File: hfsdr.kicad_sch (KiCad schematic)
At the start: 41 parts, among them U2 ADA4938-1

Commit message: wokrin
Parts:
- added C31, C32: 0.1u, Capacitor_SMD:C_0402_1005Metric, symbol Device:C
- added C33, C35, C36, C37, C38, C39, C40, C41, C42, C43, C48, C53, C54: 0.1uF, Capacitor_SMD:C_0402_1005Metric, symbol Device:C
- added C34, C44, C45, C46, C47, C49, C50: 1uF, Capacitor_SMD:C_0402_1005Metric, symbol Device:C
- added C51, C52: 0.1n, Capacitor_SMD:C_0402_1005Metric, symbol Device:C
- added R10, R12, R13: 50k, Resistor_SMD:R_0402_1005Metric, symbol Device:R_US
- added R11, R15, R16, R18, R19, R20: 10k, Resistor_SMD:R_0402_1005Metric, symbol Device:R_US
- added R14: 100, Resistor_SMD:R_0402_1005Metric, symbol Device:R_US
- added R17: 4.12k, Resistor_SMD:R_0402_1005Metric, symbol Device:R_US
- added U3: ~, symbol hfsdr:590BD80M0000DG
- added U4: AD9515, Package_CSP:LFCSP-32-1EP_5x5mm_P0.5mm_EP3.1x3.1mm, symbol Timer:AD9515
- added U5, U6: ~, symbol hfsdr:NCP110AMX180TBG
- added U7: ~, symbol hfsdr:TLV77333PDBVR
- R1: value 200 -> 402
- R2: value 120 -> 402
- R7: value 200 -> 127
- R8: value 90 -> 127
- R9: value 63.4 -> 50k
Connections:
- net DRGND is gone; now on net AGND: C19.2, C20.2, C21.2, C22.2, C23.2, C24.2, C25.2, C26.2, U1.11 (DRGND), U1.13 (DRGND), U1.17 (DRGND)
- net AGND: now also R9.2, C33.2, C34.2, C35.2, C36.2, C37.2, C38.2, C39.2, C40.2, C41.2, C42.2, C43.2, C44.2, C45.2, C46.2, C47.2, C48.1, C49.2, C50.2, R10.1, R12.2, R13.2, R17.1, U3.3 (GND), U4.10 (S7), U4.12 (S5), U4.13 (S4), U4.14 (S3), U4.15 (S2), U4.16 (S1), U4.25 (S0), U4.31 (GND), U4.33 (GND), U4.7 (S10), U4.8 (S9), U4.9 (S8), U5.B2 (GND), U6.B2 (GND), U7.2 (GND); no longer R2.1, R9.1
- net AVDD: now also C45.1, U5.A2 (OUT)
- net DRVDD: now also C47.1, U6.A2 (OUT)
- net at R8.2, U2.3 (-): now also R1.1; no longer R7.1
- net at R7.2: now also R2.1, U2.2 (+); no longer U2.1 (FB-)
- net at R3.1, U2.10: no longer R1.1
- net at U1.4 (CLK+): now also C54.1
- net at U1.5 (CLK-): now also C53.1
- net at U2.12 (~{PD}): now also R20.1
- net at U2.5 (V+), U2.6 (V+), U2.7 (V+)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: now also R20.2
- net at U2.4 (FB+): now also R2.2
- net VIN: no longer names the net of R8.1
- net VIN: no longer R9.2
- new net: C52.1, R12.1, U4.23 (OUT0)
- new net: C32.1, R10.2, U3.5 (CLK-)
- new net: R16.2, U6.B1 (EN)
- new net: C31.1, R9.1, U3.4 (CLK+)
- new net: C31.2, U4.2 (CLK)
- new net: R1.2, U2.1 (FB-)
- new net: C32.2, U4.3 (CLKB)
- new net: R18.1, U4.5 (SYNCB)
- new net: R11.1, U3.2 (OE)
- new net: C51.1, R13.1, U4.22 (OUT0B)
- new net: R17.2, U4.32 (RSET)
- new net: R15.2, U5.B1 (EN)
- new net: R19.2, U7.3 (EN)
- new net +5V: C44.1, C46.1, C49.1, R15.1, R16.1, R19.1, U5.A1 (IN), U6.A1 (IN), U7.1 (IN)
- new net CLK+: C52.2, C54.2, R14.2
- new net CLK-: C51.2, C53.2, R14.1
- new net CLKVDD: C33.1, C34.1, C35.1, C36.1, C37.1, C38.1, C39.1, C40.1, C41.1, C42.1, C43.1, C48.2, C50.1, R11.2, R18.2, U3.6 (VDD), U4.1 (VS), U4.11 (S6), U4.17 (VS), U4.20 (VS), U4.21 (VS), U4.24 (VS), U4.26 (VS), U4.29 (VS), U4.30 (VS), U4.4 (VS), U7.5 (OUT)
- no-connect marks 0 -> 4
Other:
- note added: "100 ohm diff trx line"
- note added: "10dB gain driver stage"
- note added: "input impedance of Rg * 2 for diff balanced (127)"
- note added: "term resistor close as possible"
- note added: "uhh"
- moved on the sheet: C27, C28, C29, C30, R1, R2, R3, R4, R5, R6, R7, R8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

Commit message: update
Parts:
- added C55, C60: 1uF, Capacitor_SMD:C_0402_1005Metric, symbol Device:C
- added C56, C61: 2.2uF, Capacitor_SMD:C_0402_1005Metric, symbol Device:C
- added C57, C58, C59: 0.1uF, Capacitor_SMD:C_0402_1005Metric, symbol Device:C
- added R21, R22, R23, R24, R25, R26, R27, R28: 10k, Resistor_SMD:R_0402_1005Metric, symbol Device:R_US
- added R29: 25k, Resistor_SMD:R_0402_1005Metric, symbol Device:R_US
- added R30: 50k, Resistor_SMD:R_0402_1005Metric, symbol Device:R_US
- added U10, U9: ~, Package_TO_SOT_SMD:SOT-89-3, symbol hfsdr:AP2205-50Y-13
- added U8: ~, Package_CSP:LFCSP-20-1EP_4x4mm_P0.5mm_EP2.1x2.1mm, symbol hfsdr:ADL5206
- R1, R2: value 402 -> 250
- R7, R8: value 127 -> 50
- U1: footprint (none) -> Package_CSP:LFCSP-32-1EP_5x5mm_P0.5mm_EP3.6x3.6mm_ThermalVias
- U5, U6: footprint (none) -> Package_DFN_QFN:OnSemi_XDFN4-1EP_1.0x1.0mm_EP0.52x0.52mm
- U7: footprint (none) -> Package_TO_SOT_SMD:SOT-23-5
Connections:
- net AGND: now also C55.2, C56.2, C57.2, C58.2, C59.1, C60.2, C61.2, R22.1, R24.1, R26.1, R27.1, R28.1, R30.2, U10.2 (GND), U8.0 (EP), U9.2 (GND); no longer U4.10 (S7), U4.12 (S5), U4.13 (S4), U4.14 (S3), U4.15 (S2), U4.16 (S1), U4.25 (S0), U4.7 (S10), U4.8 (S9), U4.9 (S8)
- net CLKVDD: now also R23.1; no longer C48.2, U4.11 (S6)
- net at R7.1: now also U8.15 (VOUT+)
- net -5V: now reaches U2.13 (V-), U2.14 (V-), U2.15 (V-), U2.16 (V-)
- net at R20.2, U2.5 (V+), U2.6 (V+)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: now also C61.1, U10.3 (VOUT)
- net at R8.1: now also U8.14 (VOUT-)
- net VIN+ renamed ADCIN+
- net VIN- renamed ADCIN-
- new net: R22.2, U4.10 (S7), U4.12 (S5), U4.13 (S4), U4.14 (S3), U4.15 (S2), U4.16 (S1), U4.25 (S0), U4.7 (S10), U4.8 (S9), U4.9 (S8)
- new net: R26.2, U8.11 (LATCH/SPI_HP_LP)
- new net: R21.2, U8.13 (PWUP)
- new net: R29.2, R30.1, U8.19 (VPOS)
- new net: C48.2, R23.2, U4.11 (S6)
- new net: R28.2, U8.7 (FA/GS0/D2)
- new net: C59.2, U8.1 (VCM)
- new net: R24.2, U8.2 (MODE1)
- new net: R25.2, U8.3 (MODE0)
- new net: R27.2, U8.9 (UPDN_DAT/D0/3SPI_4SPI)
- new net +13.8V: C55.1, C60.1, U10.1 (VIN), U9.1 (VIN)
- new net AMPIN+: U8.17 (VIN+)
- new net AMPIN-: U8.18 (VIN-)
- new net VGA_CSB: U8.6 (CS/GS1/D3)
- new net VGA_VDD: C56.1, C57.1, C58.1, R21.1, R25.1, R29.1, U8.16 (VPOS), U8.19 (VPOS), U9.3 (VOUT)
- no-connect marks 4 -> 5
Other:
- note added: "14dB gain driver stage"
- note added: "add filtering between amps?"
- note added: "antialias lpf"
- note added: "bpfs?"
- note added: "check the datasheet???"
- note added: "close to driver"
- note added: "input"
- note added: "input impedance of Rg * 2 for diff balanced (100)"
- note added: "place close as possible to pins"
- note added: "private ADC supply"
- note added: "pull to +5v for 4 wire"
- note added: "set up in SPI 3 wire mode"
- note removed: "10dB gain driver stage"
- note removed: "input impedance of Rg * 2 for diff balanced (127)"
- note removed: "uhh"
- moved on the sheet: C27, C28, C29, C30, C48, C51, C52, C53, C54, R1, R12, R13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

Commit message: pcb ready
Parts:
- added C62: 120p, Capacitor_SMD:C_0402_1005Metric, symbol Device:C
- added C63, C64: 200p, Capacitor_SMD:C_0402_1005Metric, symbol Device:C
- added C65: 160p, Capacitor_SMD:C_0402_1005Metric, symbol Device:C
- added C66: 470n, Capacitor_SMD:C_0402_1005Metric, symbol Device:C
- added C67, C68: 0.1u, Capacitor_SMD:C_0402_1005Metric, symbol Device:C
- added J1: RFIN, Connector_Coaxial:SMA_Amphenol_132289_EdgeMount, symbol Connector:Conn_Coaxial_Small
- added L1: 390n, Inductor_SMD:L_0402_1005Metric, symbol Device:L
- added L2: 470n, Inductor_SMD:L_0402_1005Metric, symbol Device:L
- added L3: 510n, Inductor_SMD:L_0402_1005Metric, symbol Device:L
- added L4: 300n, Inductor_SMD:L_0402_1005Metric, symbol Device:L
- U3: footprint (none) -> hfsdr:SI590_5x7mm
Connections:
- net +5V: now also U5.4 (IN), U6.4 (IN); no longer U5.A1 (IN), U6.A1 (IN)
- net AGND: now also U1.33 (AGND), U5.2 (GND), U5.5 (EP), U6.2 (GND), U6.5 (EP), U8.21 (EP), C62.2, C63.2, C64.2, C65.2, C68.1, J1.2 (Ext); no longer U1.0 (AGND), U5.B2 (GND), U6.B2 (GND), U8.0 (EP)
- net AMPIN+: now also C67.2
- net AMPIN-: now also C68.2
- net AVDD: now also U5.1 (OUT); no longer U5.A2 (OUT)
- net DRVDD: now also U6.1 (OUT); no longer U6.A2 (OUT)
- net at R16.2: now also U6.3 (EN); no longer U6.B1 (EN)
- net at R29.2, R30.1: now also U8.20 (DNC_INTERIM); no longer U8.19 (VPOS)
- net at R15.2: now also U5.3 (EN); no longer U5.B1 (EN)
- new net: C65.1, L3.2, L4.1
- new net: C62.1, C66.2, L1.1
- new net: C67.1, L4.2
- new net: C64.1, L2.2, L3.1
- new net: C66.1, J1.1 (In)
- new net: C63.1, L1.2, L2.1
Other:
- note added: "amphenol 132289"
- note removed: "antialias lpf"
- note removed: "bpfs?"
- note removed: "input"

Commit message: dgfsd
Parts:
- added C69: 0.1uF, Capacitor_SMD:C_0402_1005Metric, symbol Device:C
- U10, U9: value ~ -> AP2205-50Y-13
- U7: value ~ -> TLV77333PDBVR
- U8: value ~ -> ADL5206
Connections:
- net AGND: now also R23.1, C69.1; no longer C19.2, C20.2, C21.2, C22.2, C23.2, C24.2, C25.2, C26.2
- net CLKVDD: no longer R23.1
- net at C61.1, R20.2, U10.3 (VOUT)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: now also C69.2
- new net DRGND: C19.2, C20.2, C21.2, C22.2, C23.2, C24.2, C25.2, C26.2
- no-connect marks 5 -> 17
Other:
- moved on the sheet: R27, R28

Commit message: asd
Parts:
- removed C28, C30: 15pF, Capacitor_SMD:C_0402_1005Metric, symbol Device:C
- removed R5: 33, Resistor_SMD:R_0402_1005Metric, symbol Device:R_US
- removed R6: 15, Resistor_SMD:R_0402_1005Metric, symbol Device:R_US
- added D1: ESD9B3.3ST5G, Diode_SMD:D_SOD-923, symbol Diode:ESD9B3.3ST5G
- added L5, L6: 30n, Inductor_SMD:L_0402_1005Metric, symbol Device:L
- C29: value 5pF -> 47pF
- R3: value 33 -> 24.3
- R4: value 15 -> 24.3
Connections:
- net ADCIN+: now also C29.2, L6.2; no longer R4.2
- net ADCIN-: now also C29.1, L5.2
- net AGND: now also D1.1 (A1)
- net at U2.11: now also R4.1
- net at C66.1, J1.1 (In): now also D1.2 (A2)
- new net: L5.1, R4.2
- new net: L6.1, R3.2
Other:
- note removed: "add filtering between amps?"
- moved on the sheet: C29, C62, C63, C64, C65, C66, C67, C68, J1, L1, L2, L3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

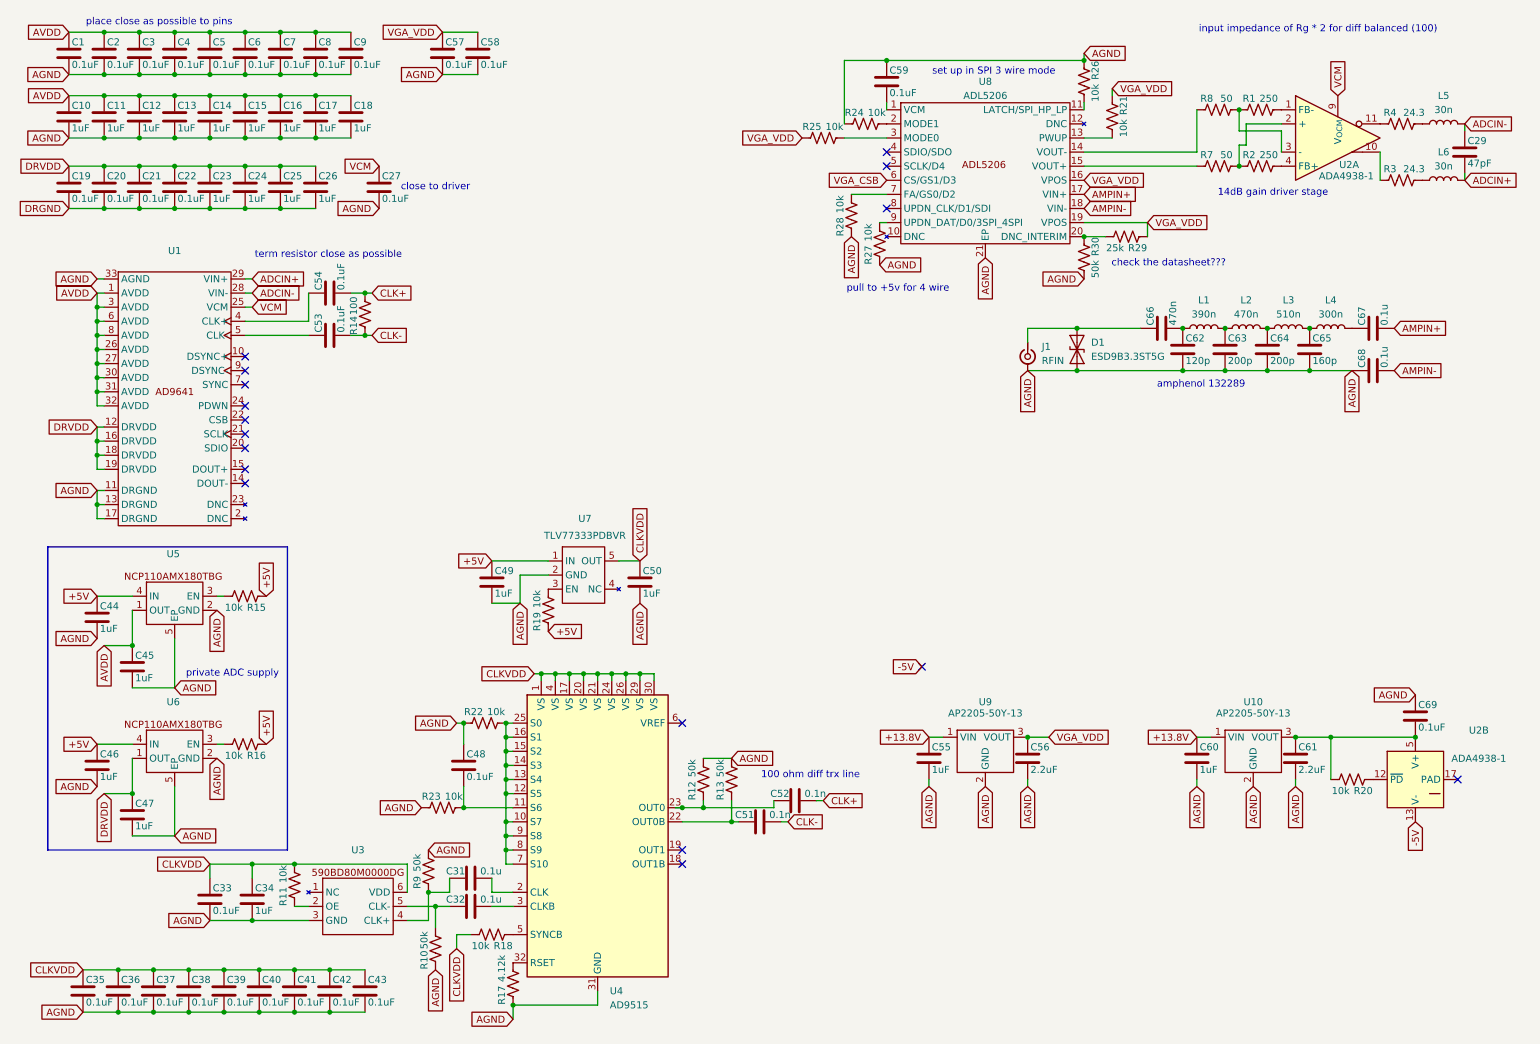
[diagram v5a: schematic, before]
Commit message: setup usbc
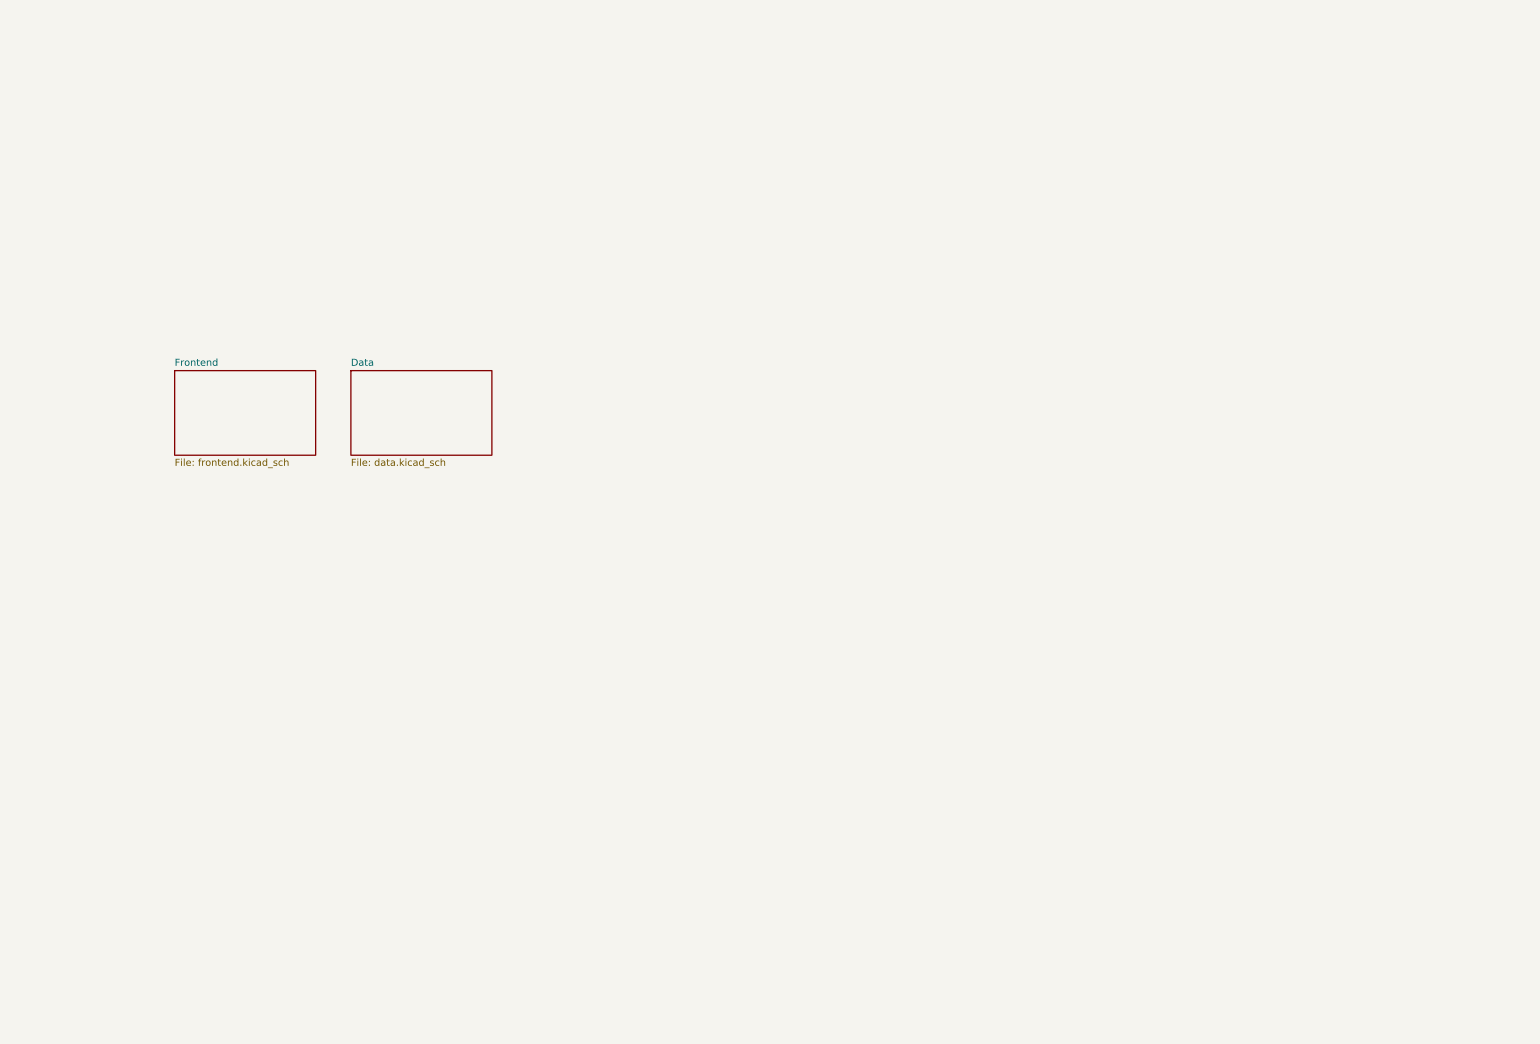
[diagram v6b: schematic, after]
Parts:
- removed C1, C19, C2, C20, C21, C22, C27, C3, C33, C35, C36, C37, C38, C39, C4, C40, C41, C42, C43, C48, C5, C53, C54, C57, C58, C59, C6, C69, C7, C8, C9: 0.1uF, Capacitor_SMD:C_0402_1005Metric, symbol Device:C
- removed C10, C11, C12, C13, C14, C15, C16, C17, C18, C23, C24, C25, C26, C34, C44, C45, C46, C47, C49, C50, C55, C60: 1uF, Capacitor_SMD:C_0402_1005Metric, symbol Device:C
- removed C29: 47pF, Capacitor_SMD:C_0402_1005Metric, symbol Device:C
- removed C31, C32, C67, C68: 0.1u, Capacitor_SMD:C_0402_1005Metric, symbol Device:C
- removed C51, C52: 0.1n, Capacitor_SMD:C_0402_1005Metric, symbol Device:C
- removed C56, C61: 2.2uF, Capacitor_SMD:C_0402_1005Metric, symbol Device:C
- removed C62: 120p, Capacitor_SMD:C_0402_1005Metric, symbol Device:C
- removed C63, C64: 200p, Capacitor_SMD:C_0402_1005Metric, symbol Device:C
- removed C65: 160p, Capacitor_SMD:C_0402_1005Metric, symbol Device:C
- removed C66: 470n, Capacitor_SMD:C_0402_1005Metric, symbol Device:C
- removed D1: ESD9B3.3ST5G, Diode_SMD:D_SOD-923, symbol Diode:ESD9B3.3ST5G
- removed J1: RFIN, Connector_Coaxial:SMA_Amphenol_132289_EdgeMount, symbol Connector:Conn_Coaxial_Small
- removed L1: 390n, Inductor_SMD:L_0402_1005Metric, symbol Device:L
- removed L2: 470n, Inductor_SMD:L_0402_1005Metric, symbol Device:L
- removed L3: 510n, Inductor_SMD:L_0402_1005Metric, symbol Device:L
- removed L4: 300n, Inductor_SMD:L_0402_1005Metric, symbol Device:L
- removed L5, L6: 30n, Inductor_SMD:L_0402_1005Metric, symbol Device:L
- removed R1, R2: 250, Resistor_SMD:R_0402_1005Metric, symbol Device:R_US
- removed R10, R12, R13, R30, R9: 50k, Resistor_SMD:R_0402_1005Metric, symbol Device:R_US
- removed R11, R15, R16, R18, R19, R20, R21, R22, R23, R24, R25, R26, R27, R28: 10k, Resistor_SMD:R_0402_1005Metric, symbol Device:R_US
- removed R14: 100, Resistor_SMD:R_0402_1005Metric, symbol Device:R_US
- removed R17: 4.12k, Resistor_SMD:R_0402_1005Metric, symbol Device:R_US
- removed R29: 25k, Resistor_SMD:R_0402_1005Metric, symbol Device:R_US
- removed R3, R4: 24.3, Resistor_SMD:R_0402_1005Metric, symbol Device:R_US
- removed R7, R8: 50, Resistor_SMD:R_0402_1005Metric, symbol Device:R_US
- removed U1: ~, Package_CSP:LFCSP-32-1EP_5x5mm_P0.5mm_EP3.6x3.6mm_ThermalVias, symbol hfsdr:AD9641
- removed U10, U9: AP2205-50Y-13, Package_TO_SOT_SMD:SOT-89-3, symbol hfsdr:AP2205-50Y-13
- removed U2: ADA4938-1, Package_CSP:LFCSP-16-1EP_3x3mm_P0.5mm_EP1.3x1.3mm_ThermalVias, symbol Amplifier_Difference:ADA4938-1
- removed U3: ~, hfsdr:SI590_5x7mm, symbol hfsdr:590BD80M0000DG
- removed U4: AD9515, Package_CSP:LFCSP-32-1EP_5x5mm_P0.5mm_EP3.1x3.1mm, symbol Timer:AD9515
- removed U5, U6: ~, Package_DFN_QFN:OnSemi_XDFN4-1EP_1.0x1.0mm_EP0.52x0.52mm, symbol hfsdr:NCP110AMX180TBG
- removed U7: TLV77333PDBVR, Package_TO_SOT_SMD:SOT-23-5, symbol hfsdr:TLV77333PDBVR
- removed U8: ADL5206, Package_CSP:LFCSP-20-1EP_4x4mm_P0.5mm_EP2.1x2.1mm, symbol hfsdr:ADL5206
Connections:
- no-connect marks 17 -> 0
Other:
- added sheet Data (data.kicad_sch)
- added sheet Frontend (frontend.kicad_sch)
- note removed: "100 ohm diff trx line"
- note removed: "14dB gain driver stage"
- note removed: "amphenol 132289"
- note removed: "check the datasheet???"
- note removed: "close to driver"
- note removed: "input impedance of Rg * 2 for diff balanced (100)"
- note removed: "place close as possible to pins"
- note removed: "private ADC supply"
- note removed: "pull to +5v for 4 wire"
- note removed: "set up in SPI 3 wire mode"
- note removed: "term resistor close as possible"

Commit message: dawg idk
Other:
- added sheet FPGA (fpga.kicad_sch)
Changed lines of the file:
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@@
+		)
+	)
+	(sheet
+		(at 41.91 100.33)
+		(size 25.4 15.24)
+		(fields_autoplaced yes)
+		(stroke
+			(width 0.1524)
+			(type solid)
+		)
+		(fill
+			(color 0 0 0 0.0000)
+		)
+		(property "Sheetname" "FPGA"
+			(at 41.91 99.6184 0)
+			(effects
+				(font
+					(size 1.27 1.27)
+				)
+				(justify left bottom)
+			)
+		)
+		(property "Sheetfile" "fpga.kicad_sch"
+			(at 41.91 116.1546 0)
+			(effects
+				(font
+					(size 1.27 1.27)
+				)
+				(justify left top)
+			)
+		)
+		(instances
+			(project "hfsdr"
+				(path "/b0f4ea81-e287-4b08-8f8c-7fcbaea1e477"
+					(page "4")
+				)
+			)
 		)
 	)

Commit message: i dont even remember what i did
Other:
- added sheet DAC (dac.kicad_sch)
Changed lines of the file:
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@@
 	(generator_version "8.0")
 	(paper "A4")
+	(wire
+		(pts
+			(xy 62.23 142.24) (xy 60.96 142.24)
+		)
+		(stroke
+			(width 0)
+			(type default)
+		)
+	)
+	(global_label "AGND"
+		(shape input)
+		(at 60.96 142.24 180)
+		(fields_autoplaced yes)
+		(effects
+			(font
+				(size 1.27 1.27)
+			)
+			(justify right)
+		)
+		(property "Intersheetrefs" "${INTERSHEET_REFS}"
+			(at 53.0157 142.24 0)
+			(effects
+				(font
+					(size 1.27 1.27)
+				)
+				(justify right)
+				(hide yes)
+			)
+		)
+	)
+	(global_label "GND"
+		(shape input)
+		(at 62.23 142.24 0)
+		(fields_autoplaced yes)
+		(effects
+			(font
+				(size 1.27 1.27)
+			)
+			(justify left)
+		)
+		(property "Intersheetrefs" "${INTERSHEET_REFS}"
+			(at 69.0857 142.24 0)
+			(effects
+				(font
+					(size 1.27 1.27)
+				)
+				(justify left)
+				(hide yes)
+			)
+		)
+	)
+	(sheet
+		(at 73.66 100.33)
+		(size 26.67 15.24)
+		(fields_autoplaced yes)
+		(stroke
+			(width 0.1524)
+			(type solid)
+		)
+		(fill
+			(color 0 0 0 0.0000)
+		)
+		(property "Sheetname" "DAC"
+			(at 73.66 99.6184 0)
+			(effects
+				(font
+					(size 1.27 1.27)
+				)
+				(justify left bottom)
+			)
+		)
+		(property "Sheetfile" "dac.kicad_sch"
+			(at 73.66 116.1546 0)
+			(effects
+				(font
+					(size 1.27 1.27)
+				)
+				(justify left top)
+			)
+		)
+		(instances
+			(project "hfsdr"
+				(path "/b0f4ea81-e287-4b08-8f8c-7fcbaea1e477"
+					(page "5")
+				)
+			)
+		)
+	)
 	(sheet
 		(at 41.91 77.47)
